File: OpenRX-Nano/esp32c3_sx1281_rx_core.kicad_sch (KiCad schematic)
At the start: 39 parts, among them U1 ESP32-C3FH4, U2 TLV75533PDQNR, U3 SX1281IMLTRT, U4 RFX2401C, X1 CJ17-400001010B20

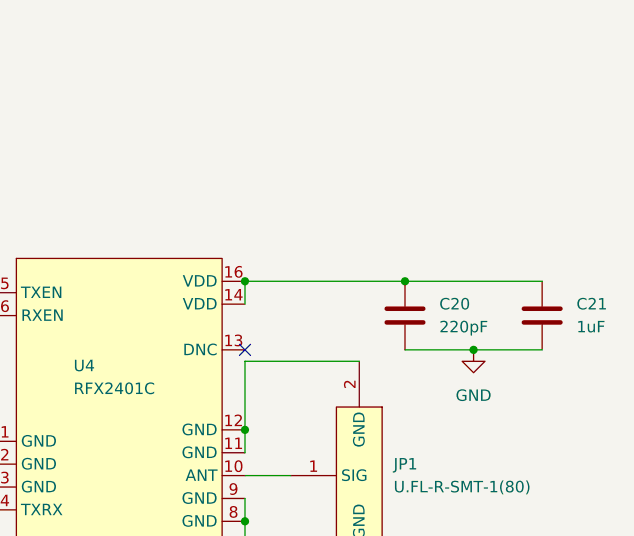
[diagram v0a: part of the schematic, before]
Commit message: Add LCSC to 220R resistor (C25092) in Dual TCXO path
220R series + 10pF DC-cut between TCXO output and LR1121 XTA
per Semtech user manual recommendation.
900 still needs this added in KiCad GUI.
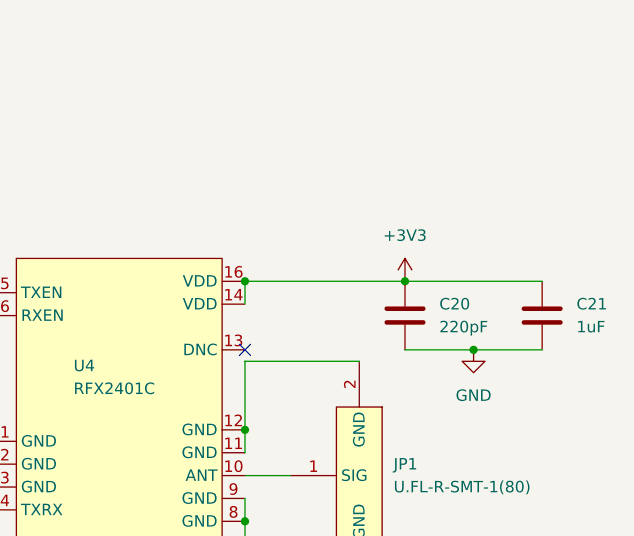
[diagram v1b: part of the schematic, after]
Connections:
- net +3V3: now also C20.1, C21.1, U4.14 (VDD), U4.16 (VDD)
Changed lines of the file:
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@@
+	)
+	(symbol
+		(lib_id "power:+3V3")
+		(at 373.38 49.53 0)
+		(unit 1)
+		(body_style 1)
+		(exclude_from_sim no)
+		(in_bom yes)
+		(on_board yes)
+		(in_pos_files yes)
+		(dnp no)
+		(fields_autoplaced yes)
+		(property "Reference" "#PWR029"
+			(at 373.38 53.34 0)
+			(hide yes)
+			(show_name no)
+			(do_not_autoplace no)
+			(effects
+				(font
+					(size 1.27 1.27)
+				)
+			)
+		)
+		(property "Value" "+3V3"
+			(at 373.38 44.45 0)
+			(show_name no)
+			(do_not_autoplace no)
+			(effects
+				(font
+					(size 1.27 1.27)
+				)
+			)
+		)
+		(property "Footprint" ""
+			(at 373.38 49.53 0)
+			(hide yes)
+			(show_name no)
+			(do_not_autoplace no)
+			(effects
+				(font
+					(size 1.27 1.27)
+				)
+			)
+		)
+		(property "Datasheet" ""
+			(at 373.38 49.53 0)
+			(hide yes)
+			(show_name no)
+			(do_not_autoplace no)
+			(effects
+				(font
+					(size 1.27 1.27)
+				)
+			)
+		)
+		(property "Description" "Power symbol creates a global label with name \"+3V3\""
+			(at 373.38 49.53 0)
+			(hide yes)
+			(show_name no)
+			(do_not_autoplace no)
+			(effects
+				(font
+					(size 1.27 1.27)
+				)
+			)
+		)
+		(pin "1"
+		)
+		(instances
+			(project "OpenRX-Nano"
+				(path "/8521861a-4fab-458b-8289-5e2efb91d906/d4225140-81df-42e7-abd7-e679e5ab5187"
+					(reference "#PWR029")
+					(unit 1)
+				)
+			)
+		)
 	)
 	(symbol

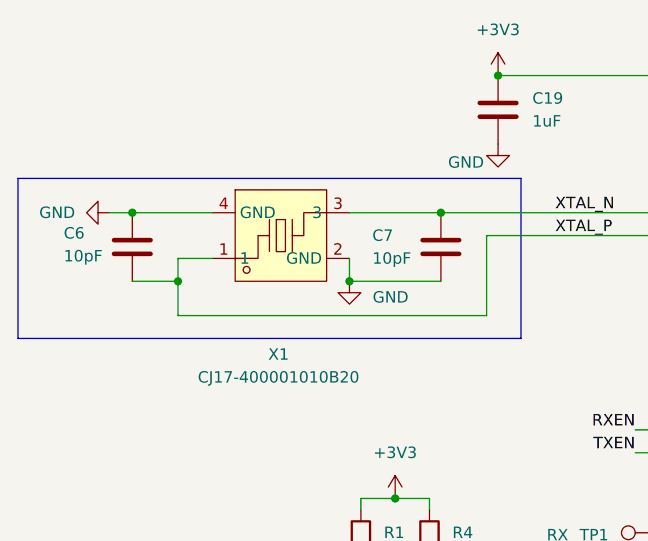
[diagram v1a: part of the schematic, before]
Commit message: Fix crystal load caps: 10pF → 18pF (C71153) on all 4 receivers
CJ17-400001010B20 crystal has CL=10pF. With 10pF load caps and
~2pF stray, effective load was only 7pF (30% low). Changed to 18pF
giving ~11pF effective load, matching the crystal spec.

C71153 = Samsung CL03C180JA3NNNC, 18pF C0G 25V 0201.
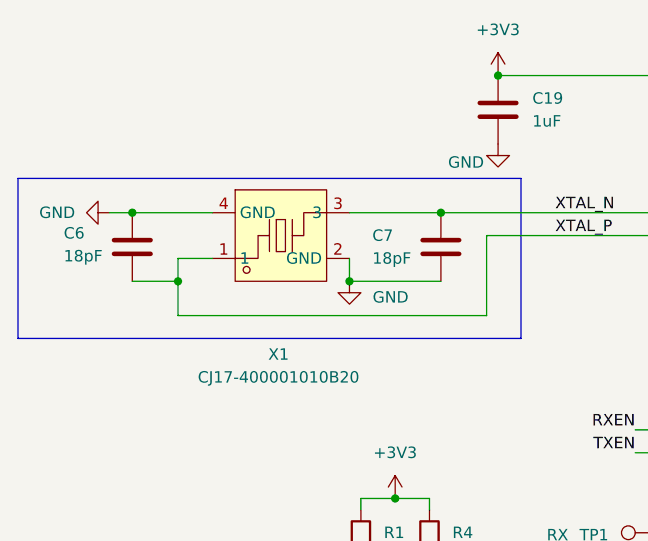
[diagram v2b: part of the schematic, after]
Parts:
- C6, C7: value 10pF -> 18pF; LCSC C14854 -> C71153
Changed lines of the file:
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@@
 			)
 		)
-		(property "Value" "10pF"
+		(property "Value" "18pF"
 			(at 66.04 46.99 0)
 			(show_name no)
@@
 			)
 		)
-		(property "LCSC" "C14854"
+		(property "LCSC" "C71153"
 			(at 0 0 0)
 			(hide yes)
@@
 			)
 		)
-		(property "Value" "10pF"
+		(property "Value" "18pF"
 			(at 31.75 46.736 0)
 			(show_name no)
@@
 			)
 		)
-		(property "LCSC" "C14854"
+		(property "LCSC" "C71153"
 			(at 0 0 0)
 			(hide yes)
